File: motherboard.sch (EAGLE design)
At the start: 134 parts, among them IC1 LM2576, IC10 TUSB2046B, IC11 OPA129U, IC2 74LS595D, IC3 74LS595D, IC4 IC_FT230X-SSOP-16, IC5 VN5772AK, IC6 VN5772AK, IC7 VN5772AK, IC8 VN5772AK, IC9 VN5772AK, U2 V_REG_LDOSMD, U3 ATMEGA168, Y1 16Mhz, Y2 6MHz

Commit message: added thermal sensors, external switches
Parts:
- added C46, C48, C52: 4.7uF, adafruit:C-USC1206
- added C47, C49, C50, C51: 0.1uF, adafruit:C-USC1206
- added C53, C54, C55, C56: 1000uF, adafruit:CPOL-US153CLV-0807
- added IC12, IC13: LM50, linear:LM50
- added JP12, JP13: (no value), SparkFun-Connectors:M063.5MM-6
- added JP14, JP15, JP16, JP17: (no value), sparkfun:M023.5MM
- added Q1, Q2, Q3, Q4: (no value), adafruit:MOSFET-NREFLOW
- added R36, R37: 10k, adafruit:R-US_R1206
- C34: value (none) -> 0.1uF
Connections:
- removed net N$46: IC3.QG
- new net N$55: JP12.5, R36.1
- new net N$56: JP13.5, R37.1
- new net N$57: JP17.2, Q4.D
- new net SW0: IC3.QE, Q1.G
- new net SW1: IC3.QF, Q2.G
- new net SW2: IC3.QG, Q3.G
- new net SW3: IC3.QH, Q4.G
- net +12V: now also C53.+, C54.+, C55.+, C56.+, JP14.1, JP15.1, JP16.1, JP17.1
- net +5V: now also C46.1, C47.1, C48.1, C49.1, C52.1, IC12.+VS, IC13.+VS, JP12.1, JP13.1
- net AGND: now also C46.2, C47.2, C48.2, C49.2, C50.2, C51.2, IC12.GND, IC13.GND
- net ARM_EN: now also R37.2
- net GND: now also C52.2, C53.-, C54.-, C55.-, C56.-, JP12.6, JP13.6, Q1.S, Q2.S, Q3.S, Q4.S
- net MISO: now also JP12.3, JP13.3
- net MOSI: now also JP12.2, JP13.2
- net N$43: now also JP14.2, Q1.D; no longer IC3.QH
- net N$47: now also JP15.2, Q2.D; no longer IC3.QF
- net N$48: now also JP16.2, Q3.D; no longer IC3.QE
- net RANG_EN: now also R36.2
- net SCK: now also JP12.4, JP13.4
- net TEMP0: now also C50.1, IC12.VO
- net TEMP1: now also C51.1, IC13.VO
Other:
- moved on the sheet: C24, C25, C26, C27, C28, C29, C3, C30, C31, C32, C33, C34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

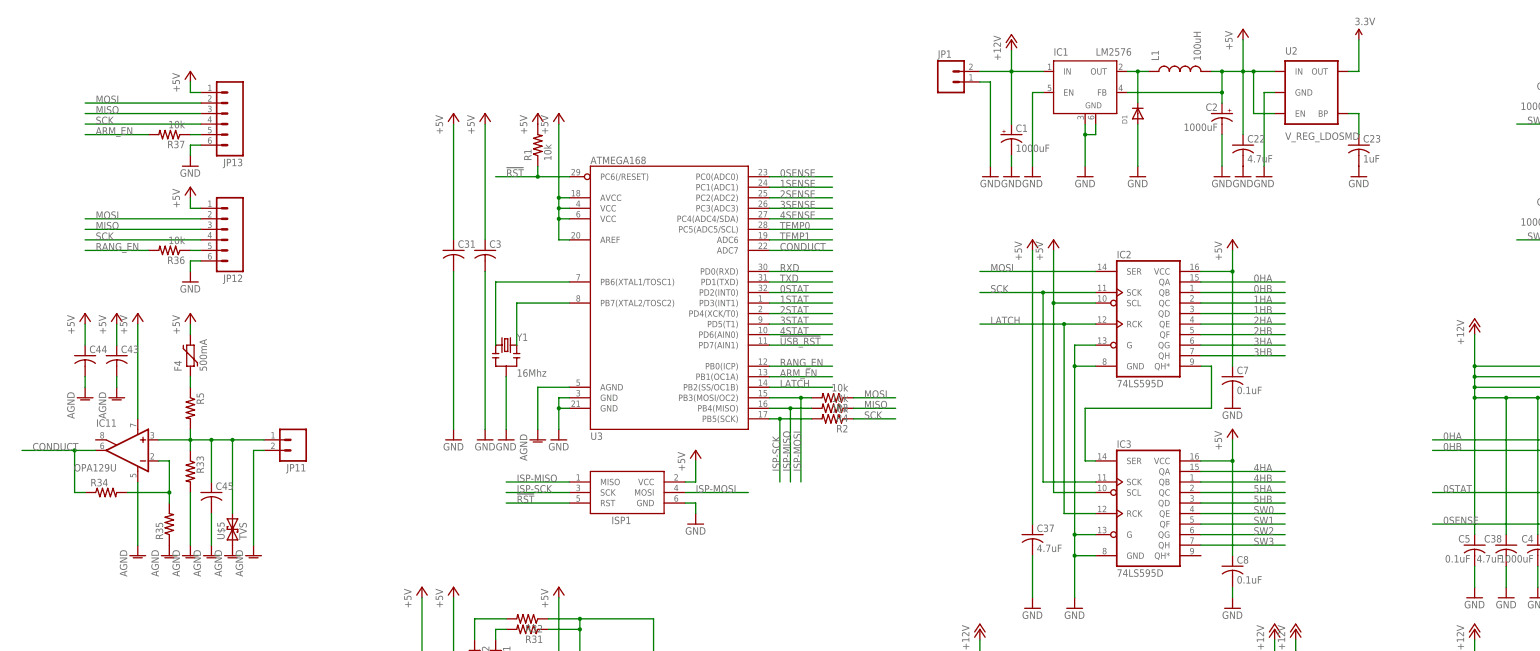
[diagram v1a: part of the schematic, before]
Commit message: fixed conductivity circuit, connected agnd->gnd
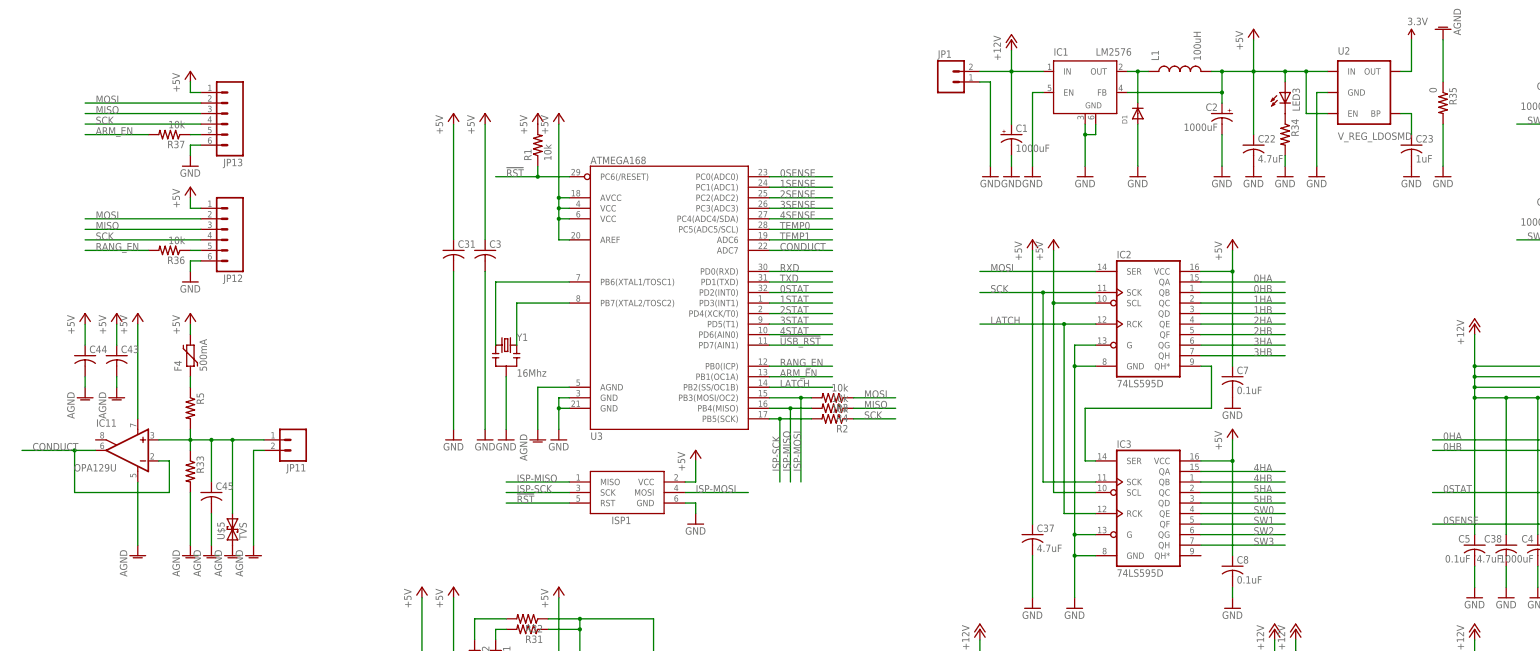
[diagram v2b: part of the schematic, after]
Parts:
- added LED3: (no value), adafruit:LEDCHIPLED_1206
- R35: value (none) -> 0
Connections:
- removed net N$54: IC11.-IN, R34.2, R35.2
- new net N$46: LED3.C, R34.1
- net +5V: now also LED3.A
- net CONDUCT: now also IC11.-IN; no longer R34.1
- net GND: now also R34.2, R35.2
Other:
- moved on the sheet: C22, C23, R34, R35, U2
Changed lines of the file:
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@@
 <?xml version="1.0" encoding="utf-8"?>
 <!DOCTYPE eagle SYSTEM "eagle.dtd">
-<eagle version="6.5.0">
+<eagle version="6.1">
 <drawing>
 <settings>
@@
 <part name="C45" library="adafruit" deviceset="C-US" device="C1206"/>
 <part name="AGND8" library="supply1" deviceset="AGND" device=""/>
-<part name="R34" library="adafruit" deviceset="R-US_" device="R1206"/>
-<part name="R35" library="adafruit" deviceset="R-US_" device="R1206"/>
-<part name="AGND9" library="supply1" deviceset="AGND" device=""/>
 <part name="IC12" library="linear" deviceset="LM50" device=""/>
 <part name="IC13" library="linear" deviceset="LM50" device=""/>
@@
 <part name="Q4" library="adafruit" deviceset="MOSFET-N" device="REFLOW"/>
 <part name="GND96" library="sparkfun" deviceset="GND" device=""/>
+<part name="LED3" library="adafruit" deviceset="LED" device="CHIPLED_1206"/>
+<part name="R34" library="adafruit" deviceset="R-US_" device="R1206"/>
+<part name="GND97" library="sparkfun" deviceset="GND" device=""/>
+<part name="GND98" library="sparkfun" deviceset="GND" device=""/>
+<part name="AGND9" library="supply1" deviceset="AGND" device=""/>
+<part name="R35" library="adafruit" deviceset="R-US_" device="R1206" value="0"/>
 </parts>
 <sheets>
@@
 <instance part="GND4" gate="1" x="320.04" y="264.16"/>
 <instance part="GND5" gate="1" x="274.32" y="264.16"/>
-<instance part="P+1" gate="1" x="325.12" y="299.72"/>
+<instance part="P+1" gate="1" x="327.66" y="299.72"/>
 <instance part="JP1" gate="G$1" x="254" y="287.02"/>
 <instance part="GND6" gate="1" x="264.16" y="264.16"/>
@@
 <instance part="GND51" gate="1" x="401.32" y="15.24"/>
 <instance part="IC10" gate="G$1" x="111.76" y="48.26"/>
-<instance part="U2" gate="G$1" x="342.9" y="284.48"/>
-<instance part="GND52" gate="1" x="330.2" y="264.16"/>
-<instance part="GND53" gate="1" x="353.06" y="264.16"/>
-<instance part="GND54" gate="1" x="325.12" y="264.16"/>
-<instance part="C22" gate="G$1" x="325.12" y="271.78"/>
-<instance part="C23" gate="G$1" x="353.06" y="271.78"/>
-<instance part="P+24" gate="G$1" x="353.06" y="297.18"/>
+<instance part="U2" gate="G$1" x="355.6" y="284.48"/>
+<instance part="GND52" gate="1" x="342.9" y="264.16"/>
+<instance part="GND53" gate="1" x="365.76" y="264.16"/>
+<instance part="GND54" gate="1" x="327.66" y="264.16"/>
+<instance part="C22" gate="G$1" x="327.66" y="271.78"/>
+<instance part="C23" gate="G$1" x="365.76" y="271.78"/>
+<instance part="P+24" gate="G$1" x="365.76" y="297.18"/>
 <instance part="P+25" gate="G$1" x="88.9" y="81.28"/>
 <instance part="P+23" gate="1" x="322.58" y="203.2"/>
@@
 <instance part="C45" gate="G$1" x="76.2" y="187.96"/>
 <instance part="AGND8" gate="VR1" x="76.2" y="172.72"/>
-<instance part="R34" gate="G$1" x="50.8" y="187.96"/>
-<instance part="R35" gate="G$1" x="66.04" y="180.34" rot="R90"/>
-<instance part="AGND9" gate="VR1" x="66.04" y="172.72"/>
 <instance part="IC12" gate="G$1" x="71.12" y="142.24"/>
 <instance part="IC13" gate="G$1" x="71.12" y="111.76"/>
@@
 <instance part="Q4" gate="G$1" x="439.42" y="251.46"/>
 <instance part="GND96" gate="1" x="441.96" y="243.84"/>
+<instance part="LED3" gate="G$1" x="335.28" y="284.48"/>
+<instance part="R34" gate="G$1" x="335.28" y="274.32" rot="R270"/>
+<instance part="GND97" gate="1" x="335.28" y="264.16"/>
+<instance part="GND98" gate="1" x="373.38" y="264.16"/>
+<instance part="AGND9" gate="VR1" x="373.38" y="299.72" rot="R180"/>
+<instance part="R35" gate="G$1" x="373.38" y="281.94" rot="R270"/>
 </instances>
 <busses>
@@
 <pinref part="U2" gate="G$1" pin="GND"/>
 <pinref part="GND52" gate="1" pin="GND"/>
-<wire x1="330.2" y1="266.7" x2="330.2" y2="284.48" width="0.1524" layer="91"/>
-<wire x1="330.2" y1="284.48" x2="332.74" y2="284.48" width="0.1524" layer="91"/>
+<wire x1="342.9" y1="266.7" x2="342.9" y2="284.48" width="0.1524" layer="91"/>
+<wire x1="342.9" y1="284.48" x2="345.44" y2="284.48" width="0.1524" layer="91"/>
 </segment>
 <segment>
@@
 <pinref part="GND96" gate="1" pin="GND"/>
 </segment>
+<segment>
+<pinref part="R34" gate="G$1" pin="2"/>
+<pinref part="GND97" gate="1" pin="GND"/>
+<wire x1="335.28" y1="266.7" x2="335.28" y2="269.24" width="0.1524" layer="91"/>
+</segment>
+<segment>
+<pinref part="GND98" gate="1" pin="GND"/>
+<pinref part="R35" gate="G$1" pin="2"/>
+<wire x1="373.38" y1="276.86" x2="373.38" y2="266.7" width="0.1524" layer="91"/>
+</segment>
 </net>
 <net name="+5V" class="0">
@@
 <junction x="320.04" y="289.56"/>
 <pinref part="P+1" gate="1" pin="+5V"/>
-<wire x1="325.12" y1="289.56" x2="325.12" y2="297.18" width="0.1524" layer="91"/>
+<wire x1="327.66" y1="289.56" x2="327.66" y2="297.18" width="0.1524" layer="91"/>
 <pinref part="U2" gate="G$1" pin="IN"/>
-<wire x1="325.12" y1="289.56" x2="327.66" y2="289.56" width="0.1524" layer="91"/>
+<wire x1="327.66" y1="289.56" x2="335.28" y2="289.56" width="0.1524" layer="91"/>
 <pinref part="C22" gate="G$1" pin="1"/>
-<wire x1="327.66" y1="289.56" x2="332.74" y2="289.56" width="0.1524" layer="91"/>
-<wire x1="325.12" y1="274.32" x2="325.12" y2="289.56" width="0.1524" layer="91"/>
+<wire x1="335.28" y1="289.56" x2="340.36" y2="289.56" width="0.1524" layer="91"/>
+<wire x1="340.36" y1="289.56" x2="345.44" y2="289.56" width="0.1524" layer="91"/>
+<wire x1="327.66" y1="274.32" x2="327.66" y2="289.56" width="0.1524" layer="91"/>
 <pinref part="U2" gate="G$1" pin="EN"/>
-<wire x1="332.74" y1="279.4" x2="327.66" y2="279.4" width="0.1524" layer="91"/>
-<wire x1="327.66" y1="279.4" x2="327.66" y2="289.56" width="0.1524" layer="91"/>
+<wire x1="345.44" y1="279.4" x2="340.36" y2="279.4" width="0.1524" layer="91"/>
+<wire x1="340.36" y1="279.4" x2="340.36" y2="289.56" width="0.1524" layer="91"/>
+<junction x="340.36" y="289.56"/>
+<wire x1="320.04" y1="289.56" x2="327.66" y2="289.56" width="0.1524" layer="91"/>
 <junction x="327.66" y="289.56"/>
-<wire x1="320.04" y1="289.56" x2="325.12" y2="289.56" width="0.1524" layer="91"/>
-<junction x="325.12" y="289.56"/>
+<pinref part="LED3" gate="G$1" pin="A"/>
+<wire x1="335.28" y1="287.02" x2="335.28" y2="289.56" width="0.1524" layer="91"/>
+<junction x="335.28" y="289.56"/>
 </segment>
 <segment>
@@
 <pinref part="U2" gate="G$1" pin="BP"/>
 <pinref part="C23" gate="G$1" pin="1"/>
-<wire x1="353.06" y1="274.32" x2="353.06" y2="279.4" width="0.1524" layer="91"/>
-<wire x1="353.06" y1="279.4" x2="350.52" y2="279.4" width="0.1524" layer="91"/>
+<wire x1="365.76" y1="274.32" x2="365.76" y2="279.4" width="0.1524" layer="91"/>
+<wire x1="365.76" y1="279.4" x2="363.22" y2="279.4" width="0.1524" layer="91"/>
 </segment>
 </net>
@@
 <pinref part="U2" gate="G$1" pin="OUT"/>
 <pinref part="P+24" gate="G$1" pin="3.3V"/>
-<wire x1="353.06" y1="297.18" x2="353.06" y2="289.56" width="0.1524" layer="91"/>
-<wire x1="353.06" y1="289.56" x2="350.52" y2="289.56" width="0.1524" layer="91"/>
+<wire x1="365.76" y1="297.18" x2="365.76" y2="289.56" width="0.1524" layer="91"/>
+<wire x1="365.76" y1="289.56" x2="363.22" y2="289.56" width="0.1524" layer="91"/>
 </segment>
 <segment>
@@
 </segment>
 <segment>
-<pinref part="R35" gate="G$1" pin="1"/>
-<pinref part="AGND9" gate="VR1" pin="AGND"/>
-</segment>
-<segment>
 <pinref part="IC12" gate="G$1" pin="GND"/>
 <pinref part="AGND10" gate="VR1" pin="AGND"/>
@@
 <pinref part="C50" gate="G$1" pin="2"/>
 </segment>
+<segment>
+<pinref part="AGND9" gate="VR1" pin="AGND"/>
+<pinref part="R35" gate="G$1" pin="1"/>
+<wire x1="373.38" y1="287.02" x2="373.38" y2="297.18" width="0.1524" layer="91"/>
+</segment>
 </net>
 <net name="N$2" class="0">
@@
 <wire x1="48.26" y1="198.12" x2="43.18" y2="198.12" width="0.1524" layer="91"/>
 <label x="33.02" y="198.12" size="1.778" layer="95"/>
-<pinref part="R34" gate="G$1" pin="1"/>
 <wire x1="43.18" y1="198.12" x2="30.48" y2="198.12" width="0.1524" layer="91"/>
-<wire x1="45.72" y1="187.96" x2="43.18" y2="187.96" width="0.1524" layer="91"/>
 <wire x1="43.18" y1="187.96" x2="43.18" y2="198.12" width="0.1524" layer="91"/>
 <junction x="43.18" y="198.12"/>
+<pinref part="IC11" gate="G$1" pin="-IN"/>
+<wire x1="63.5" y1="195.58" x2="66.04" y2="195.58" width="0.1524" layer="91"/>
+<wire x1="66.04" y1="195.58" x2="66.04" y2="187.96" width="0.1524" layer="91"/>
+<wire x1="43.18" y1="187.96" x2="66.04" y2="187.96" width="0.1524" layer="91"/>
 </segment>
 </net>
@@
 </segment>
 </net>
-<net name="N$54" class="0">
-<segment>
-<pinref part="IC11" gate="G$1" pin="-IN"/>
-<wire x1="63.5" y1="195.58" x2="66.04" y2="195.58" width="0.1524" layer="91"/>
-<wire x1="66.04" y1="195.58" x2="66.04" y2="187.96" width="0.1524" layer="91"/>
-<wire x1="66.04" y1="187.96" x2="55.88" y2="187.96" width="0.1524" layer="91"/>
-<pinref part="R34" gate="G$1" pin="2"/>
-<junction x="66.04" y="187.96"/>
-<pinref part="R35" gate="G$1" pin="2"/>
-<wire x1="66.04" y1="185.42" x2="66.04" y2="187.96" width="0.1524" layer="91"/>
-</segment>
-</net>
 <net name="N$55" class="0">
 <segment>
@@
 </segment>
 </net>
+<net name="N$46" class="0">
+<segment>
+<pinref part="LED3" gate="G$1" pin="C"/>
+<pinref part="R34" gate="G$1" pin="1"/>
+</segment>
+</net>

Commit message: validating subcomponents
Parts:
- removed C23: 1uF, adafruit:C-USC1206
- C3: value (none) -> 0.1uF
- C31: value (none) -> 4.7uF
- R34: value (none) -> 500
- U2: value V_REG_LDOSMD -> NCP4625
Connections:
- removed net N$20: C23.1, U2.BP
- net GND: no longer C23.2
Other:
- moved on the sheet: C22, LED3, R34, R35
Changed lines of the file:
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@@
 <part name="R1" library="adafruit" deviceset="R-US_" device="R1206" value="10k"/>
 <part name="P+4" library="supply1" deviceset="+5V" device=""/>
-<part name="C3" library="adafruit" deviceset="C-US" device="C1206"/>
+<part name="C3" library="adafruit" deviceset="C-US" device="C1206" value="0.1uF"/>
 <part name="GND10" library="sparkfun" deviceset="GND" device=""/>
 <part name="ISP1" library="adafruit" deviceset="AVRISP" device="-6"/>
@@
 <part name="GND51" library="sparkfun" deviceset="GND" device=""/>
 <part name="IC10" library="rov_club" deviceset="TUSB2046B" device=""/>
-<part name="U2" library="sparkfun" deviceset="V_REG_LDO" device="SMD"/>
+<part name="U2" library="sparkfun" deviceset="V_REG_LDO" device="SMD" value="NCP4625"/>
 <part name="GND52" library="sparkfun" deviceset="GND" device=""/>
-<part name="GND53" library="sparkfun" deviceset="GND" device=""/>
 <part name="GND54" library="sparkfun" deviceset="GND" device=""/>
 <part name="C22" library="adafruit" deviceset="C-US" device="C1206" value="4.7uF"/>
-<part name="C23" library="adafruit" deviceset="C-US" device="C1206" value="1uF"/>
 <part name="P+24" library="sparkfun" deviceset="3.3V" device=""/>
 <part name="P+25" library="sparkfun" deviceset="3.3V" device=""/>
@@
 <part name="GND71" library="sparkfun" deviceset="GND" device=""/>
 <part name="P+3" library="supply1" deviceset="+5V" device=""/>
-<part name="C31" library="adafruit" deviceset="C-US" device="C1206"/>
+<part name="C31" library="adafruit" deviceset="C-US" device="C1206" value="4.7uF"/>
 <part name="GND72" library="sparkfun" deviceset="GND" device=""/>
 <part name="P+29" library="supply1" deviceset="+5V" device=""/>
@@
 <part name="GND96" library="sparkfun" deviceset="GND" device=""/>
 <part name="LED3" library="adafruit" deviceset="LED" device="CHIPLED_1206"/>
-<part name="R34" library="adafruit" deviceset="R-US_" device="R1206"/>
+<part name="R34" library="adafruit" deviceset="R-US_" device="R1206" value="500"/>
 <part name="GND97" library="sparkfun" deviceset="GND" device=""/>
 <part name="GND98" library="sparkfun" deviceset="GND" device=""/>
@@
 <sheet>
 <plain>
+<rectangle x1="129.54" y1="175.26" x2="243.84" y2="292.1" layer="97"/>
+<rectangle x1="246.38" y1="256.54" x2="370.84" y2="304.8" layer="97"/>
+<rectangle x1="259.08" y1="157.48" x2="337.82" y2="251.46" layer="97"/>
+<rectangle x1="40.64" y1="91.44" x2="99.06" y2="152.4" layer="97"/>
 </plain>
 <instances>
@@
 <instance part="U2" gate="G$1" x="355.6" y="284.48"/>
 <instance part="GND52" gate="1" x="342.9" y="264.16"/>
-<instance part="GND53" gate="1" x="365.76" y="264.16"/>
-<instance part="GND54" gate="1" x="327.66" y="264.16"/>
-<instance part="C22" gate="G$1" x="327.66" y="271.78"/>
-<instance part="C23" gate="G$1" x="365.76" y="271.78"/>
+<instance part="GND54" gate="1" x="335.28" y="264.16"/>
+<instance part="C22" gate="G$1" x="335.28" y="271.78"/>
 <instance part="P+24" gate="G$1" x="365.76" y="297.18"/>
 <instance part="P+25" gate="G$1" x="88.9" y="81.28"/>
@@
 <instance part="Q4" gate="G$1" x="439.42" y="251.46"/>
 <instance part="GND96" gate="1" x="441.96" y="243.84"/>
-<instance part="LED3" gate="G$1" x="335.28" y="284.48"/>
-<instance part="R34" gate="G$1" x="335.28" y="274.32" rot="R270"/>
-<instance part="GND97" gate="1" x="335.28" y="264.16"/>
-<instance part="GND98" gate="1" x="373.38" y="264.16"/>
-<instance part="AGND9" gate="VR1" x="373.38" y="299.72" rot="R180"/>
-<instance part="R35" gate="G$1" x="373.38" y="281.94" rot="R270"/>
+<instance part="LED3" gate="G$1" x="327.66" y="284.48"/>
+<instance part="R34" gate="G$1" x="327.66" y="274.32" rot="R270"/>
+<instance part="GND97" gate="1" x="327.66" y="264.16"/>
+<instance part="GND98" gate="1" x="347.98" y="264.16"/>
+<instance part="AGND9" gate="VR1" x="363.22" y="264.16"/>
+<instance part="R35" gate="G$1" x="355.6" y="269.24" rot="R180"/>
 </instances>
 <busses>
@@
 </segment>
 <segment>
-<pinref part="C23" gate="G$1" pin="2"/>
-<pinref part="GND53" gate="1" pin="GND"/>
-</segment>
-<segment>
 <pinref part="IC2" gate="A" pin="GND"/>
 <wire x1="289.56" y1="218.44" x2="284.48" y2="218.44" width="0.1524" layer="91"/>
@@
 <pinref part="R34" gate="G$1" pin="2"/>
 <pinref part="GND97" gate="1" pin="GND"/>
-<wire x1="335.28" y1="266.7" x2="335.28" y2="269.24" width="0.1524" layer="91"/>
+<wire x1="327.66" y1="266.7" x2="327.66" y2="269.24" width="0.1524" layer="91"/>
 </segment>
 <segment>
 <pinref part="GND98" gate="1" pin="GND"/>
 <pinref part="R35" gate="G$1" pin="2"/>
-<wire x1="373.38" y1="276.86" x2="373.38" y2="266.7" width="0.1524" layer="91"/>
+<wire x1="350.52" y1="269.24" x2="347.98" y2="269.24" width="0.1524" layer="91"/>
+<wire x1="347.98" y1="269.24" x2="347.98" y2="266.7" width="0.1524" layer="91"/>
 </segment>
 </net>
@@
 <wire x1="327.66" y1="289.56" x2="327.66" y2="297.18" width="0.1524" layer="91"/>
 <pinref part="U2" gate="G$1" pin="IN"/>
+<pinref part="C22" gate="G$1" pin="1"/>
 <wire x1="327.66" y1="289.56" x2="335.28" y2="289.56" width="0.1524" layer="91"/>
-<pinref part="C22" gate="G$1" pin="1"/>
 <wire x1="335.28" y1="289.56" x2="340.36" y2="289.56" width="0.1524" layer="91"/>
 <wire x1="340.36" y1="289.56" x2="345.44" y2="289.56" width="0.1524" layer="91"/>
-<wire x1="327.66" y1="274.32" x2="327.66" y2="289.56" width="0.1524" layer="91"/>
+<wire x1="335.28" y1="274.32" x2="335.28" y2="289.56" width="0.1524" layer="91"/>
+<wire x1="335.28" y1="289.56" x2="327.66" y2="289.56" width="0.1524" layer="91"/>
 <pinref part="U2" gate="G$1" pin="EN"/>
 <wire x1="345.44" y1="279.4" x2="340.36" y2="279.4" width="0.1524" layer="91"/>
@@
 <junction x="327.66" y="289.56"/>
 <pinref part="LED3" gate="G$1" pin="A"/>
-<wire x1="335.28" y1="287.02" x2="335.28" y2="289.56" width="0.1524" layer="91"/>
+<wire x1="327.66" y1="287.02" x2="327.66" y2="289.56" width="0.1524" layer="91"/>
+<junction x="327.66" y="289.56"/>
 <junction x="335.28" y="289.56"/>
 </segment>
@@
 </segment>
 </net>
-<net name="N$20" class="0">
-<segment>
-<pinref part="U2" gate="G$1" pin="BP"/>
-<pinref part="C23" gate="G$1" pin="1"/>
-<wire x1="365.76" y1="274.32" x2="365.76" y2="279.4" width="0.1524" layer="91"/>
-<wire x1="365.76" y1="279.4" x2="363.22" y2="279.4" width="0.1524" layer="91"/>
-</segment>
-</net>
 <net name="3.3V" class="0">
 <segment>
@@
 <pinref part="AGND9" gate="VR1" pin="AGND"/>
 <pinref part="R35" gate="G$1" pin="1"/>
-<wire x1="373.38" y1="287.02" x2="373.38" y2="297.18" width="0.1524" layer="91"/>
-</segment>
-</net>
+<wire x1="360.68" y1="269.24" x2="363.22" y2="269.24" width="0.1524" layer="91"/>
+<wire x1="363.22" y1="269.24" x2="363.22" y2="266.7" width="0.1524" layer="91"/>
+</segment>
+</net>
